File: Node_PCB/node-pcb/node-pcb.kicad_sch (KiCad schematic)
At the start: 37 parts, among them J1 TYPE-C-31-M-12, J2 TSW-102-07-G-S, J3 TSW-118-07-L-D, J4 TSW-118-07-L-D, U1 NCP1117ST33T3G, U3 RP2040, U4 W25Q32JVSSIQ, X1 12MHz

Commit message: Remove lock files and add new datasheets and images for display components and RS485 schematic
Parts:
- removed C10, C8: 1u, RPI_COMPILED:generic_capc1005x50, symbol RPI_DB:Capacitors | MLCC | M1005/RP-01GYSK-L7FEKV
- removed C11, C12, C13, C14, C15, C16, C5, C6, C7, C9: 100n, RPI_COMPILED:generic_capc1005x50, symbol RPI_DB:Capacitors | MLCC | M1005/RP-01BJ9Y-KRGF41
- removed C2, C3: 15p, RPI_COMPILED:generic_capc1005x50, symbol RPI_DB:Capacitors | MLCC | M1005/RP-01C89W-LLY9XV
- removed J2: TSW-102-07-G-S, RPI_COMPILED:samtec_tsw-102-07-g-s, symbol RPI_DB:Connectors | Pin_Headers/RP-01JV5X-LY21H5
- removed J3, J4: TSW-118-07-L-D, RPI_COMPILED:samtec_tsw-118-07-l-d, symbol RPI_DB:Connectors | Pin_Headers/RP-01JWH2-G371Y4
- removed R1, R5: 1k, RPI_COMPILED:generic_resc1005x35, symbol RPI_DB:Resistors | Chip | M1005/RP-019A1P-4Z6ZWY
- removed R2: 10k, RPI_COMPILED:generic_resc1005x35, symbol RPI_DB:Resistors | Chip | M1005/RP-019A1P-53DHSX
- removed R3, R4: 27, RPI_COMPILED:generic_resc1005x35, symbol RPI_DB:Resistors | Chip | M1005/RP-01C89V-LTEYC4
- added C10, C19, C8: 1uF, EasyEDA:C0402, symbol EasyEDA:CL05A105KA5NQNC
- added C11, C12, C13, C14, C15, C16, C18, C5, C6, C7, C9: 100nF, EasyEDA:C0402, symbol EasyEDA:CL05B104KO5NNNC
- added C2, C3: 15pF, EasyEDA:C0402, symbol EasyEDA:0402CG150J500NT
- added J2, J3: SM06B-GHS-TB, EasyEDA:CONN-TH_SM06B-GHS-TB-LF-SN, symbol EasyEDA:SM06B-GHS-TB
- added J4: TC2030, Connector:Tag-Connect_TC2030-IDC-NL_2x03_P1.27mm_Vertical, symbol Connector:TC2030
- added J5: AFC11-S12ICA-00, EasyEDA:CONN-SMD-12P_AFC11-S12ICA-00, symbol EasyEDA:AFC11-S12ICA-00
- added Q1: S8050, EasyEDA:SOT-23-3_L3.0-W1.7-P0.95-LS2.9-BR, symbol EasyEDA:S8050_C2146
- added R1, R5: 1k, EasyEDA:R0402, symbol EasyEDA:0402WGF1001TCE
- added R10, R2, R6, R9: 10k, EasyEDA:R0402, symbol EasyEDA:0402WGF1002TCE
- added R11: 2.2k, EasyEDA:R0402, symbol EasyEDA:0402WGF2201TCE
- added R3, R4: 33, EasyEDA:R0402, symbol EasyEDA:0402WGF330JTCE
- added SW1: TS-1187A-B-A-B, EasyEDA:SW-SMD_4P-L5.1-W5.1-P3.70-LS6.5-TL_H1.5, symbol EasyEDA:TS-1187A-B-A-B
- added U4: THVD1450DR, EasyEDA:SOIC-8_L4.9-W3.9-P1.27-LS6.0-BL, symbol Interface_UART:THVD1450DR
- X1: value 12MHz -> ABM8-272-T3; footprint RPI_COMPILED:generic_xtalcc320x250x80-4 -> EasyEDA:CRYSTAL-SMD_4P-L3.2-W2.5-BL; LCSC Part (none) -> C20625731; Manufacturer (none) -> Abracon; esr 50R Max -> (none); freq_stability 30ppm -> (none); frequency 12MHz -> (none); load_capacitance 10pF -> (none); manufacturer Abracon -> (none); manufacturer_pn ABM8-272-T3 -> (none); operating_temp_max +85C -> (none); operating_temp_min -40C -> (none); package M3225 -> (none); packaging 180mm dia. tape & reel -> (none); packaging_qty 3000 -> (none); part_uid RP-01G8X7-GS352B -> (none); size 3.2x2.5x0.8mm -> (none); tolerance 30ppm -> (none); z_height_nom 0.8mm -> (none)
- renumbered U4 to U2
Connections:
- net +1V1: now also C6.1, C7.1, C8.1
- net +3V3: now also U2.8 (VCC), C10.1, C11.1, C12.1, C13.1, C14.1, C15.1, C16.1, C18.2, C19.2, C5.1, C9.1, J4.1, J5.5, R2.1, U4.8 (VCC)
- net GND: now also U2.4 (GND), C10.2, C11.2, C12.2, C13.2, C14.2, C15.2, C16.2, C18.1, C19.1, C2.1, C3.1, C5.2, C6.2, C7.2, C8.2, C9.2, J2.5, J2.6, J2.7, J2.8, J3.5, J3.6, J3.7, J3.8, J4.3, J4.6, J5.1, J5.12, J5.13, J5.14, J5.2, J5.6, Q1.2 (E), R10.2, R6.2, R9.2, SW1.4 (D), U4.5 (GND)
- net QSPI_SCLK: now also U2.6 (CLK)
- net QSPI_SD0: now also U2.5 (DI/IO_{0})
- net QSPI_SD1: now also U2.2 (DO/IO_{1})
- net QSPI_SD2: now also U2.3 (~{WP}/IO_{2})
- net QSPI_SD3: now also U2.7 (~{HOLD}/~{RESET}/IO_{3})
- net QSPI_SS: now also U2.1 (~{CS}), R1.2, R2.2
- net RUN: now also J4.5
- net SWCLK: now also J4.4
- net USB_D+: now also J1.A6 (D+), R3.2; no longer J1.B7 (D-)
- net USB_D-: now also J1.B7 (D-), R4.2; no longer J1.A6 (D+)
- net VBUS +5V: now also J2.1, J2.2, J3.1, J3.2, J5.4
- net XIN: now also C2.2
- net XOUT: now also R5.2
- net ~{USB_BOOT}: now also R1.1, SW1.2 (B)
- net at U3.46 (USB_DM): now also R4.1
- net at U3.47 (USB_DP): now also R3.1
- net at X1.3: now also C3.2, R5.1
- net GPIO12 renamed GPIO12_TX
- net GPIO12_TX: now also U4.4 (DI)
- net GPIO13 renamed GPIO13_RX
- net GPIO13_RX: now also U4.1 (RO)
- net GPIO14 renamed GPIO14_RE
- net GPIO14_RE: now also R9.1, U4.2 (~{RE})
- net GPIO15 renamed GPIO15_DE
- net GPIO15_DE: now also R6.1, U4.3 (DE)
- net GPIO16 renamed RESET
- net RESET: now also J5.11
- net GPIO17 renamed D/C
- net D/C: now also J5.7
- net GPIO18 renamed SPI0_SCK (SCL)
- net SPI0_SCK (SCL): now also J5.9
- net GPIO19 renamed SPI0_TX (MOSI)
- net SPI0_TX (MOSI): now also J5.10
- net GPIO20 renamed CS
- net CS: now also J5.8
- net GPIO21 renamed BL_PWM
- net BL_PWM: now also R11.1
- net SWD renamed SWDIO
- net SWDIO: now also J4.2
- new net: Q1.1 (B), R10.1, R11.2
- new net LEDK: J5.3, Q1.3 (C)
- new net RS485_A: J2.3, J3.3, U4.6 (A)
- new net RS485_B: J2.4, J3.4, U4.7 (B)
- no-connect marks 2 -> 4
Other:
- note added: "Crystal oscillator"
- note added: "Daisy chain connector"
- note added: "Decoupling capacitors for RP2040"
- note added: "Flash storage"
- note added: "Place C18 as close as possible to pin 8. Place C19 on the same 3V3 feed immediately upstream of C18, within 5 mm."
- note added: "Power supply"
- note added: "RP2040"
- note added: "RS485"
- note added: "SPI display"
- note added: "SWD Debug"
- note added: "Use at least two vias for VCC and ground connections of decoupling capacitors."
- note removed: "Crystal"
- note removed: "Flash"
- note removed: "IOs"
- note removed: "Power"
- moved on the sheet: C17, U2, X1

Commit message: Update pcb schematic
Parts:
- removed J2, J3: SM06B-GHS-TB, EasyEDA:CONN-TH_SM06B-GHS-TB-LF-SN, symbol EasyEDA:SM06B-GHS-TB
- added C20: 10uF, EasyEDA:C0805, symbol EasyEDA:GRM21BR61C106KE15L
- added J2, J3: BM08B-GHS-TBT, EasyEDA:CONN-SMD_BM08B-GHS-TBT-LF-SN, symbol EasyEDA:BM08B-GHS-TBT
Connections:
- net GND: now also C20.1, J2.1, J2.10, J2.4, J2.9, J3.1, J3.10, J3.4, J3.9
- net RS485_A: now also J2.5, J3.5
- net RS485_B: now also J2.6, J3.6
- net VBUS +5V: now also C20.2, J2.2, J2.3, J3.2, J3.3
- net GPIO10 renamed ADDR_OUT
- net ADDR_OUT: now also J2.7
- net GPIO11 renamed ADDR_IN
- net ADDR_IN: now also J3.7
- net GPIO8 renamed SPARE_OUT
- net SPARE_OUT: now also J2.8
- net GPIO9 renamed SPARE_IN
- net SPARE_IN: now also J3.8
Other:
- note added: "Keep QSPI traces as short as possible"
- note added: "Place crystal as close as possible to RP2040"

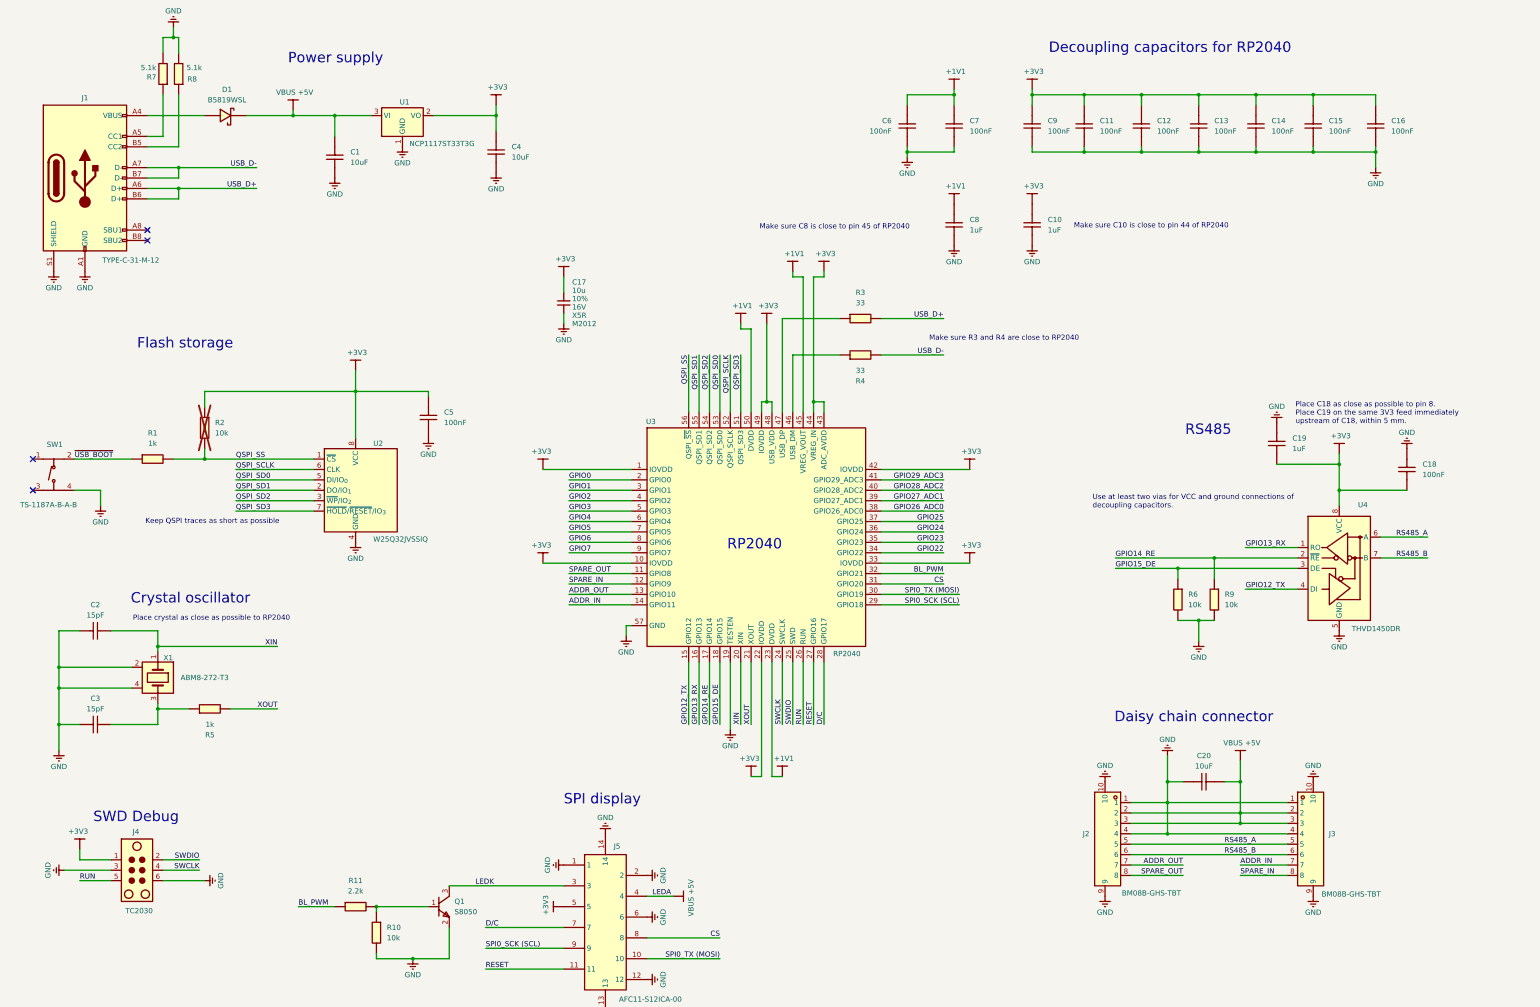
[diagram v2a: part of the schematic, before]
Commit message: Add schematic diagrams and images for Node PCB
- Added schematic.pdf for overall PCB design.
- Included schematic-connector.png for connector details.
- Added schematic-debug.png for debugging interface.
- Updated schematic-rs485.png with new changes.
- Introduced schematic-spi.png for SPI interface representation.
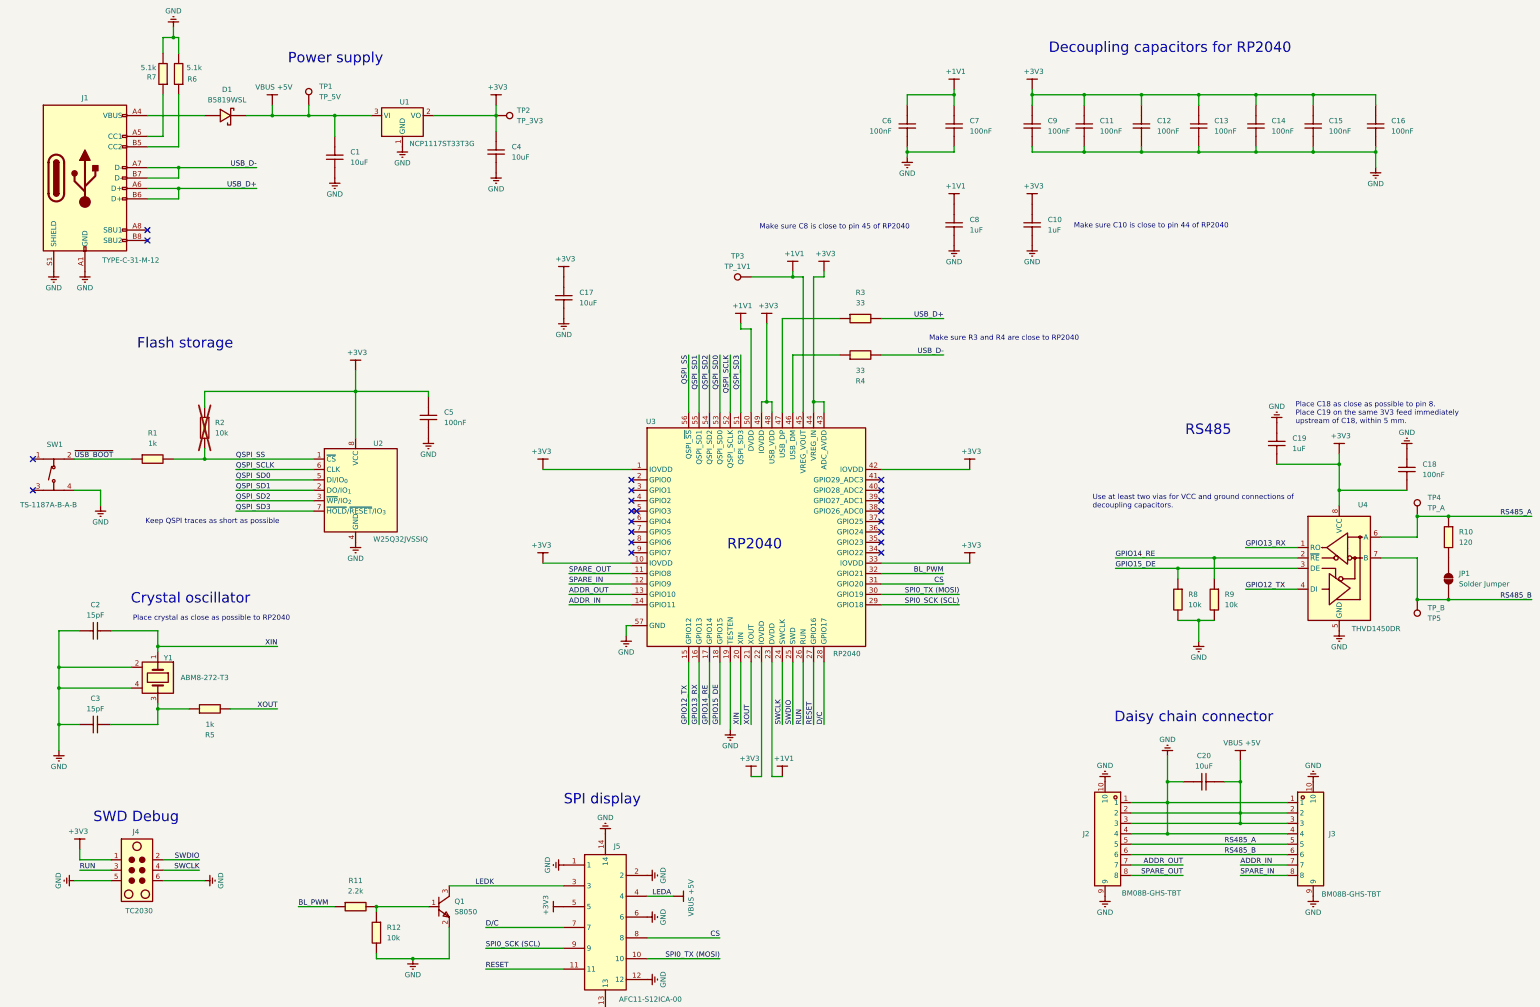
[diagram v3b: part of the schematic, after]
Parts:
- removed C17: 10u, RPI_COMPILED:generic_capc2012x125, symbol RPI_DB:Capacitors | MLCC | M2012/RP-01GYSK-AVBE41
- added C17: 10uF, EasyEDA:C0805, symbol EasyEDA:GRM21BR61C106KE15L
- added JP1: Solder Jumper, Jumper:SolderJumper-2_P1.3mm_Open_RoundedPad1.0x1.5mm, symbol Jumper:SolderJumper_2_Open
- added R10: 120, EasyEDA:R0402, symbol JLC_Import:0402WGF1200TCE
- added TP1: TP_5V, TestPoint:TestPoint_Pad_D1.0mm, symbol Connector:TestPoint
- added TP2: TP_3V3, TestPoint:TestPoint_Pad_D1.0mm, symbol Connector:TestPoint
- added TP3: TP_1V1, TestPoint:TestPoint_Pad_D1.0mm, symbol Connector:TestPoint
- added TP4: TP_A, TestPoint:TestPoint_Pad_D1.0mm, symbol Connector:TestPoint
- added TP5: TP_B, TestPoint:TestPoint_Pad_D1.0mm, symbol Connector:TestPoint
- renumbered R10 to R12, R8 to R6, R6 to R8, X1 to Y1
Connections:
- net +1V1: now also TP3.1
- net +3V3: now also C17.1, TP2.1
- net GND: now also J4.5, C17.2; no longer J4.3
- net RS485_A: now also R10.1, TP4.1
- net RS485_B: now also JP1.2 (B), TP5.1
- net RUN: now also J4.3; no longer J4.5
- net VBUS +5V: now also TP1.1
- net GPIO0: no longer names the net of U3.2 (GPIO0)
- net GPIO1: no longer names the net of U3.3 (GPIO1)
- net GPIO2: no longer names the net of U3.4 (GPIO2)
- net GPIO22: no longer names the net of U3.34 (GPIO22)
- net GPIO23: no longer names the net of U3.35 (GPIO23)
- net GPIO24: no longer names the net of U3.36 (GPIO24)
- net GPIO25: no longer names the net of U3.37 (GPIO25)
- net GPIO26_ADC0: no longer names the net of U3.38 (GPIO26_ADC0)
- net GPIO27_ADC1: no longer names the net of U3.39 (GPIO27_ADC1)
- net GPIO28_ADC2: no longer names the net of U3.40 (GPIO28_ADC2)
- net GPIO29_ADC3: no longer names the net of U3.41 (GPIO29_ADC3)
- net GPIO3: no longer names the net of U3.5 (GPIO3)
- net GPIO4: no longer names the net of U3.6 (GPIO4)
- net GPIO5: no longer names the net of U3.7 (GPIO5)
- net GPIO6: no longer names the net of U3.8 (GPIO6)
- net GPIO7: no longer names the net of U3.9 (GPIO7)
- new net: JP1.1 (A), R10.2
- no-connect marks 4 -> 21

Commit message: Add new datasheets and images; update test documentation
- Added Schottky diode datasheet (B5817W-589W) to the documentation.
- Included a simplified PSU circuit image for reference.
- Added an image illustrating the voltage drop across a Schottky diode.
- Updated the existing wiring diagram image.
- Enhanced the test README with a new section on PCB prototype design, outlining objectives for testing resistance, current, and voltage.
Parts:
- added D2: B5819WSL, EasyEDA:SOD-123_L2.7-W1.6-LS3.7-RD-1, symbol EasyEDA:B5819W_C8598
- C1, C17, C20, C4: Manufacturer muRata(村田) -> Murata Electronics; manufacturer_pn (none) -> GRM21BR61C106KE15L; package (none) -> 0805; temp_coefficient (none) -> X5R; tolerance (none) -> ± 10%; voltage (none) -> 16V
- C10, C19, C8: Manufacturer SAMSUNG(三星) -> Samsung Electro-Mechanics; manufacturer_pn (none) -> CL05A105KA5NQNC; package (none) -> 0402; temp_coefficient (none) -> X5R; tolerance (none) -> ± 10%; voltage (none) -> 25V
- C11, C12, C13, C14, C15, C16, C18, C5, C6, C7, C9: Manufacturer SAMSUNG(三星) -> Samsung Electro-Mechanics; manufacturer_pn (none) -> CL05B104KO5NNNC; package (none) -> 0402; temp_coefficient (none) -> X7R; tolerance (none) -> ± 10%; voltage (none) -> 16V
- C2, C3: Manufacturer FH(风华) -> FH (Guangdong Fenghua Advanced Tech); manufacturer_pn (none) -> 0402CG150J500NT; package (none) -> 0402; temp_coefficient (none) -> C0G; tolerance (none) -> ± 5%; voltage (none) -> 50V
- D1: manufacturer_pn (none) -> B5819W SL; package (none) -> SOD-123
- J1: manufacturer_pn (none) -> TYPE-C-31-M-12
- J2, J3: value BM08B-GHS-TBT -> BM08B-GHS-TBT(LF)(SN); manufacturer_pn (none) -> BM08B-GHS-TBT(LF)(SN); package (none) -> SMD,P=1.25mm
- J5: Manufacturer JS(钜硕电子) -> JUSHUO; manufacturer_pn (none) -> AFC11-S12ICA-00; package (none) -> SMD,P=0.5mm
- Q1: Manufacturer CJ(江苏长电/长晶) -> Jiangsu Changjing Electronics Technology Co., Ltd.; manufacturer_pn (none) -> S8050 J3Y(RANGE:200-350); package (none) -> SOT-23
- R1, R5: Manufacturer UNI-ROYAL(厚声) -> UNI-ROYAL(Uniroyal Elec); manufacturer_pn (none) -> 0402WGF1001TCE; package (none) -> 0402; power (none) -> 62.5mW; temp_coefficient (none) -> ±100ppm/℃; tolerance (none) -> ± 1%; voltage (none) -> 50V
- R10: Manufacturer UNI-ROYAL(厚声) -> UNI-ROYAL(Uniroyal Elec); manufacturer_pn (none) -> 0402WGF1200TCE; package (none) -> 0402; power (none) -> 62.5mW; temp_coefficient (none) -> ±100ppm/℃; tolerance (none) -> ± 1%; voltage (none) -> 50V
- R11: Manufacturer UNI-ROYAL(厚声) -> UNI-ROYAL(Uniroyal Elec); manufacturer_pn (none) -> 0402WGF2201TCE; package (none) -> 0402; power (none) -> 62.5mW; temp_coefficient (none) -> ±100ppm/℃; tolerance (none) -> ± 1%; voltage (none) -> 50V
- R12, R8, R9: Manufacturer UNI-ROYAL(厚声) -> UNI-ROYAL(Uniroyal Elec); manufacturer_pn (none) -> 0402WGF1002TCE; package (none) -> 0402; power (none) -> 62.5mW; temp_coefficient (none) -> ±100ppm/℃; tolerance (none) -> ± 1%; voltage (none) -> 50V
- R3, R4: Manufacturer UNI-ROYAL(厚声) -> UNI-ROYAL(Uniroyal Elec); manufacturer_pn (none) -> 0402WGF330JTCE; package (none) -> 0402; power (none) -> 62.5mW; temp_coefficient (none) -> ±100ppm/℃; tolerance (none) -> ± 1%; voltage (none) -> 50V
- R6, R7: Manufacturer UNI-ROYAL(厚声) -> UNI-ROYAL(Uniroyal Elec); manufacturer_pn (none) -> 0603WAF5101T5E; power (none) -> 100mW; temp_coefficient (none) -> ±100ppm/℃; tolerance (none) -> ± 1%; voltage (none) -> 75V
- SW1: Manufacturer XKB Connection(中国星坤) -> XKB Connection; manufacturer_pn (none) -> TS-1187A-B-A-B; package (none) -> SMD-4P,5.1x5.1mm
- TP1, TP2, TP3, TP4, TP5: now left out of the parts list
- U1: Manufacturer (none) -> onsemi; manufacturer_pn (none) -> NCP1117ST33T3G; package (none) -> SOT-223
- U2: LCSC Part (none) -> C179173; LSCS Part C179173 -> (none); manufacturer_pn (none) -> W25Q32JVSSIQ; package (none) -> SOIC-8-208mil
- U3: LCSC Part (none) -> C2040; LCSC Part # C2040 -> (none); Manufacturer (none) -> Raspberry Pi; package QFN-56 -> LQFN-56
- U4: LCSC Part (none) -> C2671361; manufacturer_pn (none) -> THVD1450DR; package (none) -> SOIC-8
- Y1: Manufacturer Abracon -> Abracon LLC; manufacturer_pn (none) -> ABM8-272-T3; package (none) -> SMD3225-4P
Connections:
- net VBUS +5V: now also D2.2 (+); no longer C1.1, D1.1 (-), TP1.1, U1.3 (VI)
- new net: C1.1, D1.1 (-), D2.1 (-), TP1.1, U1.3 (VI)
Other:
- moved on the sheet: C10, C11, C12, C13, C14, C15, C16, C17, C18, C19, C20, C6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
